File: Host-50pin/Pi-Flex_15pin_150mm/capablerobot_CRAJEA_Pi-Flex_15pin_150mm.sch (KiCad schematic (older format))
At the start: 7 parts, among them J1 WE_686715100001_FLEX, J2 WE_687650100002_FLEX, Q1 BSS138APW, Q2 BSS138APW

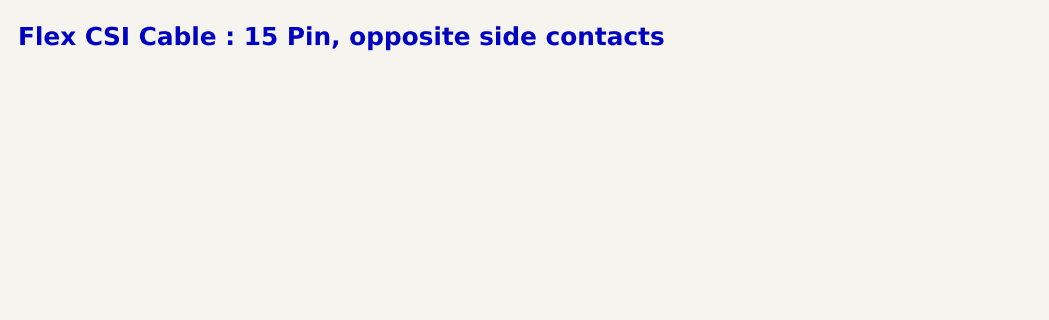
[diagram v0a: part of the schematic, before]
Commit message: Fix title block
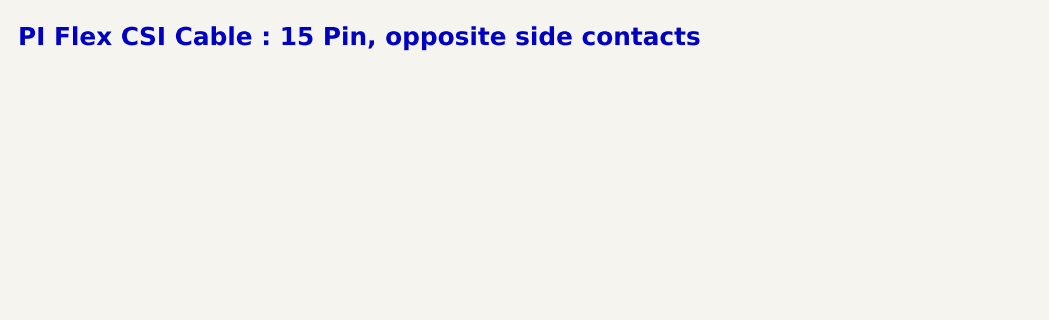
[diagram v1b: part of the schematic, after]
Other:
- note added: "PI Flex CSI Cable : 15 Pin, opposite side contacts"
- note removed: "Flex CSI Cable : 15 Pin, opposite side contacts"
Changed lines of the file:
@@
 encoding utf-8
 Sheet 1 1
-Title "Alvium flex CSI adapter 100mm double opposite side contacts"
+Title "PI Flex Cable : 15 pin, 150mm"
 Date ""
 Rev "1.0.0"
@@
 Antmicro CSI interface
 Text Notes 700  825  0    79   ~ 16
-Flex CSI Cable : 15 Pin, opposite side contacts
+PI Flex CSI Cable : 15 Pin, opposite side contacts
 $Comp
 L antmicro-alvium-flex-csi-adapter:oshw_logo N1
